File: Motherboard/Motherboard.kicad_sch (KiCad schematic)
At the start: 57 parts, among them J1 40-pin IDE Connector, J3 Bus_ISA_8bit, J4 ATX-24, J5 USB_B, J6 ATF15XX_JTAG_ISP, J7 Bus_ISA_8bit, J8 65SIB_Connector, SW1 SW_Push, SW2 SW_SPST, U1 AS6C8008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

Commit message: 307 unrouted traces...
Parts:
- D7: value LED -> HDD_ACT
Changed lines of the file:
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@@
       (effects (font (size 1.27 1.27)))
     )
-    (property "Value" "LED" (at 495.6175 331.47 0)
+    (property "Value" "HDD_ACT" (at 495.6175 331.47 0)
       (effects (font (size 1.27 1.27)))
     )

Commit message: 268 unrouted traces...
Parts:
- U19: footprint (none) -> Package_DIP:DIP-20_W7.62mm_Socket_LongPads
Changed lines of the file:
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@@
       (effects (font (size 1.27 1.27)) (justify left))
     )
-    (property "Footprint" "" (at 231.14 250.19 0)
+    (property "Footprint" "Package_DIP:DIP-20_W7.62mm_Socket_LongPads" (at 231.14 250.19 0)
       (effects (font (size 1.27 1.27)) hide)
     )

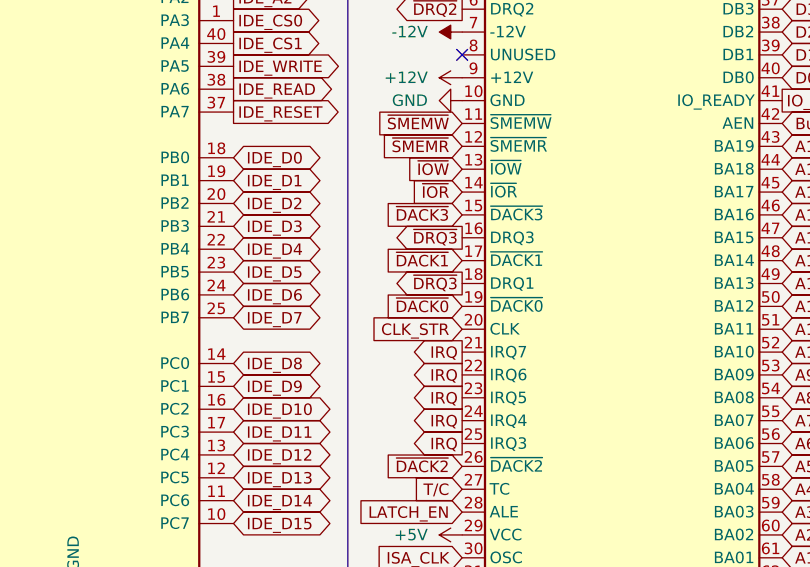
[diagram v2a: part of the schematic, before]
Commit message: Fixed DRQ1 line...
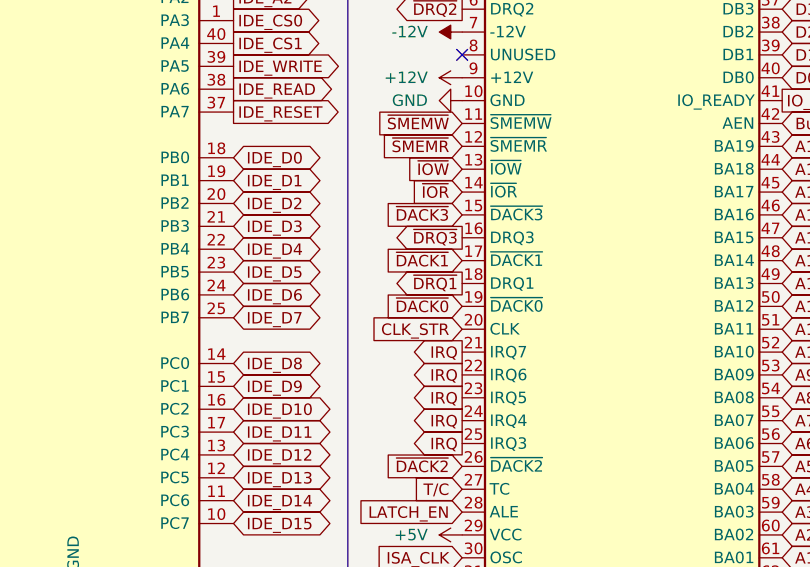
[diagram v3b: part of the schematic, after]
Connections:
- net ~{DRQ1}: now also J3.18 (DRQ1)
- net ~{DRQ3}: no longer J3.18 (DRQ1)
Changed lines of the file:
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@@
     )
   )
-  (global_label "~{DRQ3}" (shape output) (at 308.61 196.85 180) (fields_autoplaced)
+  (global_label "~{DRQ1}" (shape output) (at 308.61 196.85 180) (fields_autoplaced)
     (effects (font (size 1.27 1.27)) (justify right))
-    (property "Intersheetrefs" "${INTERSHEET_REFS}" (at 301.1169 196.7706 0)
+    (property "Intersheetrefs" "${INTERSHEET_REFS}" (at 300.6242 196.85 0)
       (effects (font (size 1.27 1.27)) (justify right) hide)
     )

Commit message: Update Motherboard.kicad_sch
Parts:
- R14: footprint (none) -> Resistor_THT:R_Axial_DIN0207_L6.3mm_D2.5mm_P7.62mm_Horizontal
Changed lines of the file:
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@@
       (effects (font (size 1.27 1.27)) (justify right))
     )
-    (property "Footprint" "" (at 139.7 76.962 90)
+    (property "Footprint" "Resistor_THT:R_Axial_DIN0207_L6.3mm_D2.5mm_P7.62mm_Horizontal" (at 139.7 76.962 90)
       (effects (font (size 1.27 1.27)) hide)
     )

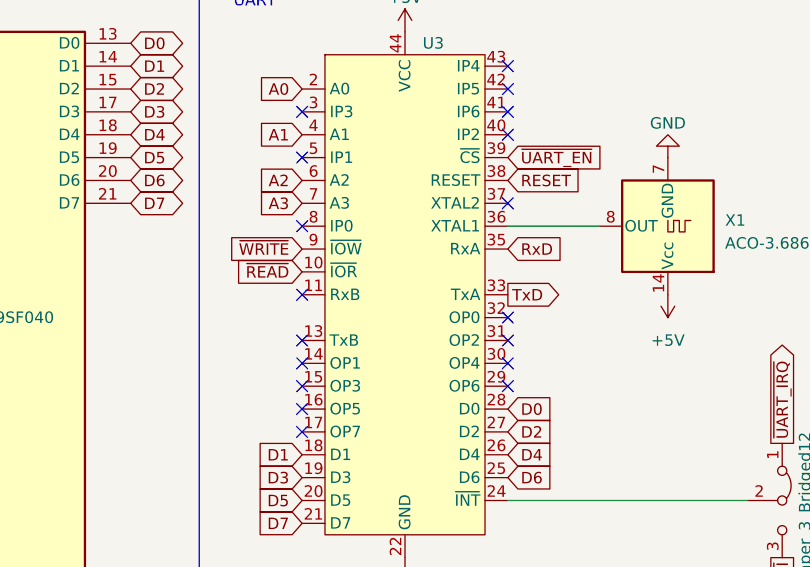
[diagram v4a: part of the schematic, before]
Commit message: Update Motherboard.kicad_sch
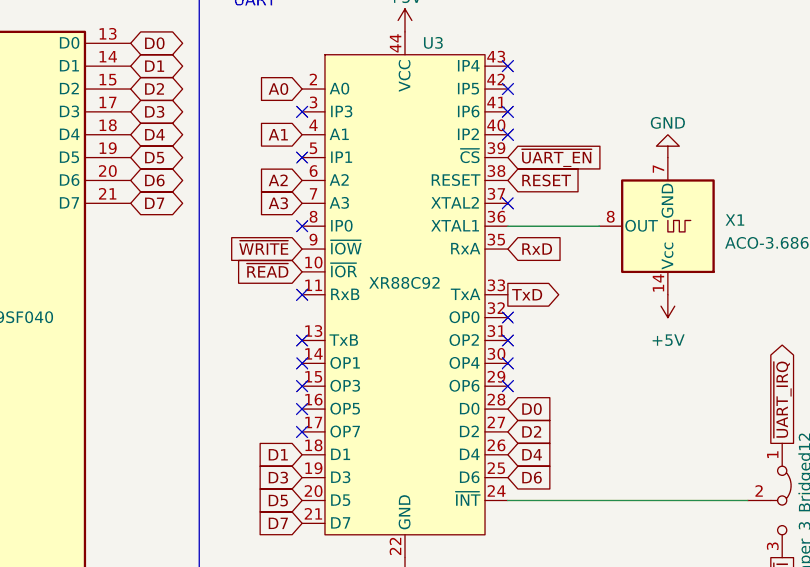
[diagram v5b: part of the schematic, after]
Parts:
- U3: value ~ -> XR88C92
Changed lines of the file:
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@@
   )
   (symbol (lib_id "UART:XR88C92") (at 462.28 76.2 0) (unit 1)
-    (in_bom yes) (on_board yes) (dnp no) (fields_autoplaced)
+    (in_bom yes) (on_board yes) (dnp no)
     (property "Reference" "U3" (at 464.2359 77.47 0)
       (effects (font (size 1.27 1.27)) (justify left))
     )
-    (property "Value" "~" (at 462.28 76.2 0)
+    (property "Value" "XR88C92" (at 462.28 104.14 0)
       (effects (font (size 1.27 1.27)))
     )
